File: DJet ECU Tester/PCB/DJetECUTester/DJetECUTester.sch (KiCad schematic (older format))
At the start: 27 parts, among them J1 ISP, J10 ECU3, J2 ECU1, J4 BREAKOUT, J5 12V IN, J6 MPS, J8 INJECTORS, J9 ECU2, U1 ATmega328P, Y1 FA-238 16.0000MB-C3

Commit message: Working on new schematic diagram.
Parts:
- removed D1: RED, LED_SMD:LED_PLCC-2, symbol Device:LED
- removed J4: BREAKOUT, Connector_PinHeader_2.54mm:PinHeader_2x13_P2.54mm_Vertical, symbol Connector_Generic:Conn_02x13_Odd_Even
- removed J8: INJECTORS, Britishideas:PhoenixContact_COMBICON_PT_5, symbol Connector:Screw_Terminal_01x05
- removed R5: 1K, Resistor_SMD:R_0805_2012Metric, symbol Device:R
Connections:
- net labels added: MCU_INJGROUP1-3, MCU_INJGROUP2-4, MCU_INJGROUP3-5, MCU_INJGROUP4-6
- net labels removed: ECU_DIAGGROUP13-25, START, STATUS, VAC1, VAC2
- wire segments 188 -> 159
- no-connect marks 3 -> 1
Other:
- moved on the sheet: J1, J2, J5, J6, TP5, TP6, TP7, TP8, TP9

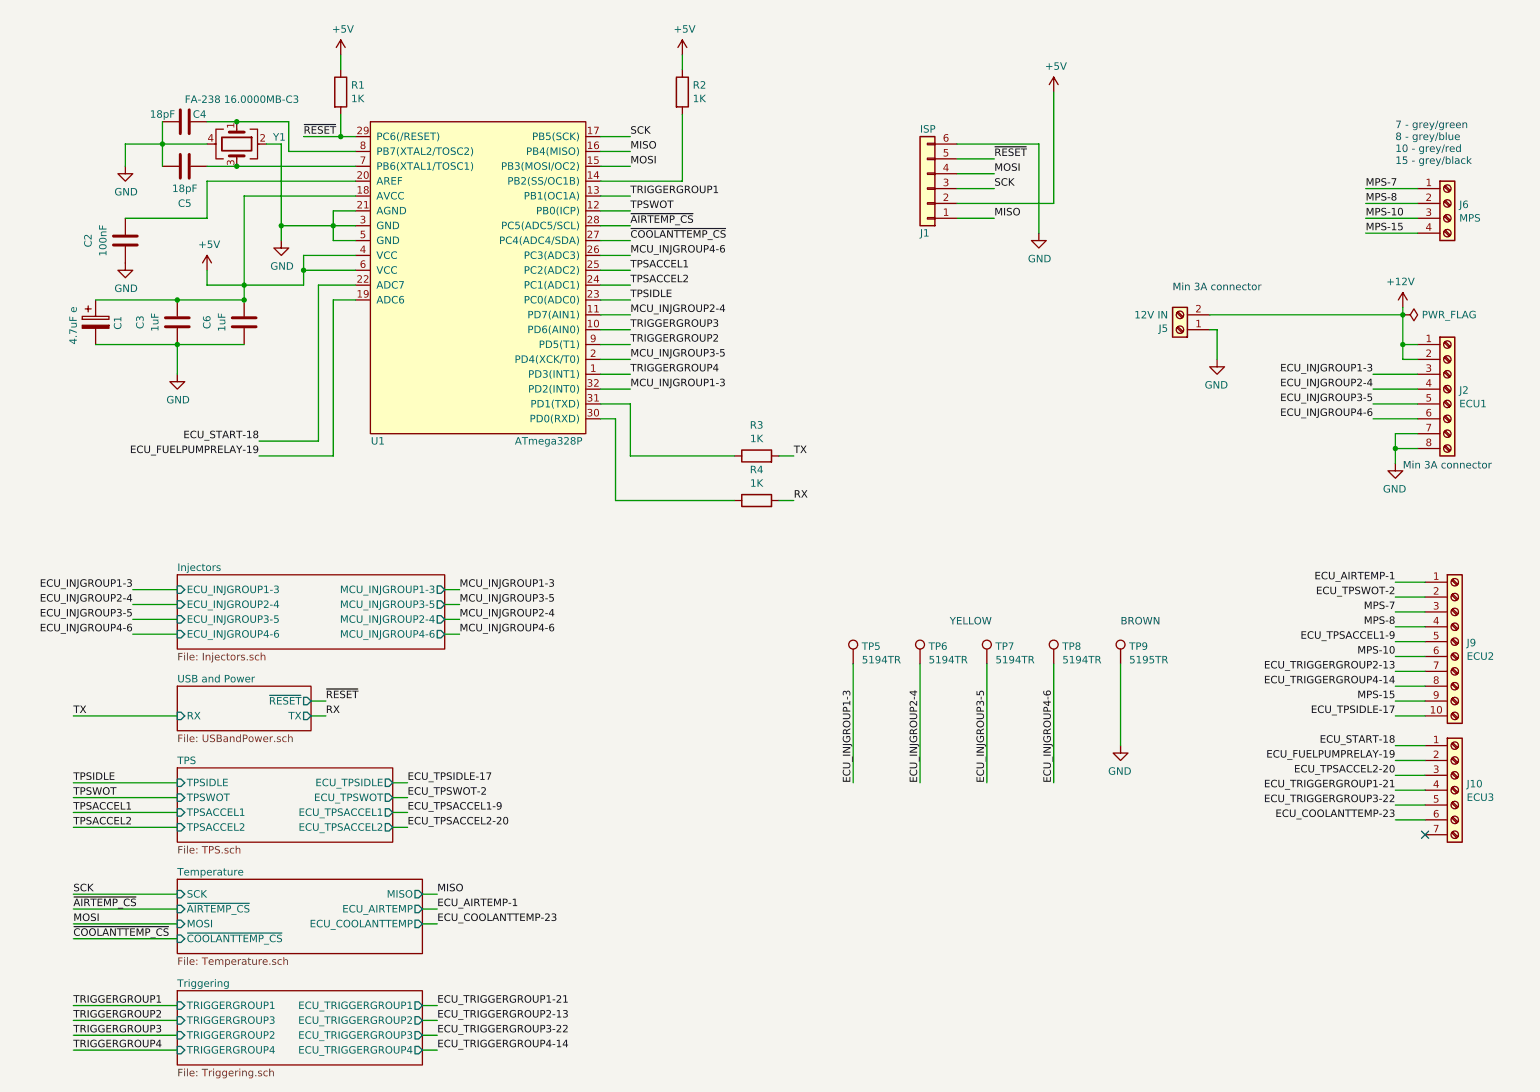
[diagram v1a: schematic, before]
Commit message: Added IO multiplexer. Working on additional coolant temperature options. Added status LED back in.
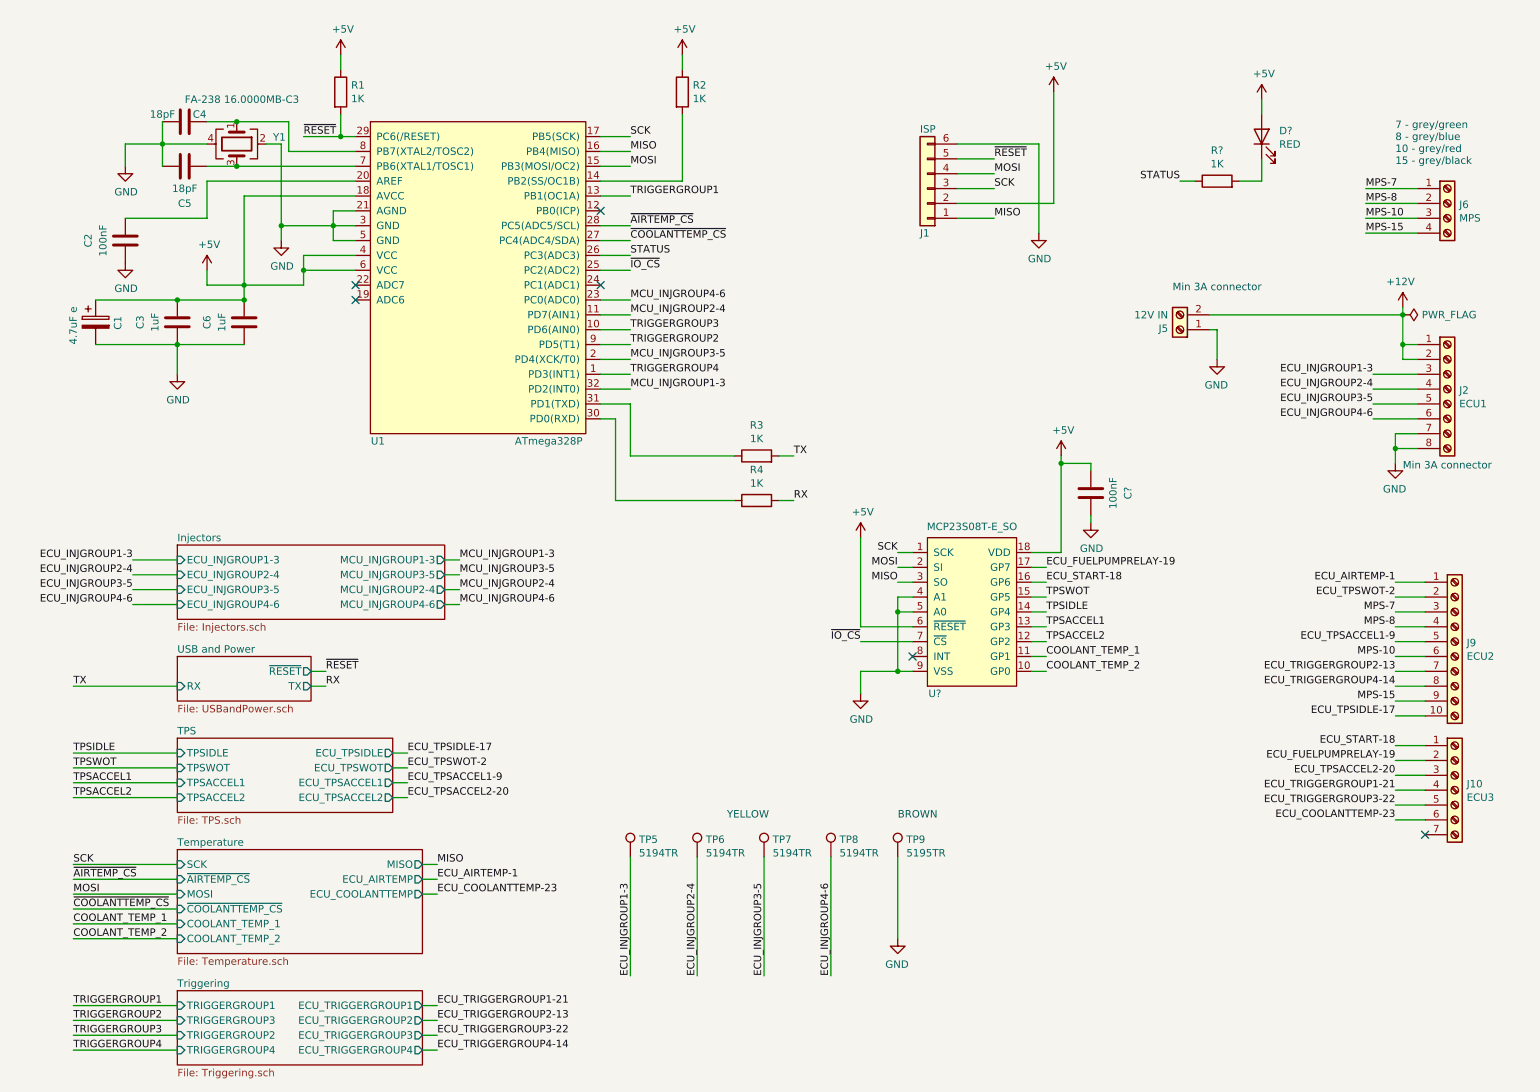
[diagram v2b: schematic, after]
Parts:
- added C?: 100nF, Capacitor_SMD:C_0805_2012Metric, symbol Device:C
- added D?: RED, LED_SMD:LED_PLCC-2, symbol Device:LED
- added R?: 1K, Resistor_SMD:R_0805_2012Metric, symbol Device:R
- added U?: MCP23S08T-E_SO, Package_SO:SOIC-18W_7.5x11.6mm_P1.27mm, symbol BritishIdeas:MCP23S08T-E_SO
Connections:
- net +5V: now also C?.2, D?.2 (A), U?.18 (VDD), U?.6 (~RESET)
- net ECU_FUELPUMPRELAY-19: now also U?.17 (GP7); no longer U1.19 (ADC6)
- net ECU_START-18: now also U?.16 (GP6); no longer U1.22 (ADC7)
- net GND: now also C?.1, U?.4 (A1), U?.5 (A0), U?.9 (VSS)
- net MCU_INJGROUP4-6: now also U1.23 (PC0(ADC0)); no longer U1.26 (PC3(ADC3))
- net MISO: now also U?.3 (SO)
- net MOSI: now also U?.2 (SI)
- net SCK: now also U?.1 (SCK)
- net TPSACCEL1: now also U?.13 (GP3); no longer U1.25 (PC2(ADC2))
- net TPSACCEL2: now also U?.12 (GP2); no longer U1.24 (PC1(ADC1))
- net TPSIDLE: now also U?.14 (GP4); no longer U1.23 (PC0(ADC0))
- net TPSWOT: now also U?.15 (GP5); no longer U1.12 (PB0(ICP))
- new net: D?.1 (K), R?.2
- new net COOLANT_TEMP_1: U?.11 (GP1)
- new net COOLANT_TEMP_2: U?.10 (GP0)
- new net STATUS: R?.1, U1.26 (PC3(ADC3))
- new net ~IO_CS: U1.25 (PC2(ADC2)), U?.7 (~CS)
- no-connect marks 1 -> 6
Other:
- moved on the sheet: TP5, TP6, TP7, TP8, TP9

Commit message: Completed new schematic.
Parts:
- added D10, D9: MBR0520LT1G, Britishideas:SOD-123, symbol Device:D
- added J4: 12V 4A IN (5.5/2.5), Connector_BarrelJack:BarrelJack_Wuerth_6941xx301002, symbol Connector:Barrel_Jack_Switch
- added R48, R49: 4k2, Resistor_SMD:R_0805_2012Metric, symbol Device:R
- added R52, R53: 10k, Resistor_SMD:R_0805_2012Metric, symbol Device:R
- gave numbers to parts that had none: 4
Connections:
- net +12V: now also J4.1
- net ECU_FUELPUMPRELAY-19: now also D10.2 (A); no longer U6.17 (GP7)
- net ECU_START-18: now also D9.2 (A); no longer U6.16 (GP6)
- net GND: now also J4.2, J4.3, R48.1, R49.1
- net ~COOLANTTEMP2_CS: now reaches U1.12 (PB0(ICP))
- net COOLANT_TEMP_1: no longer names the net of U6.11 (GP1)
- net COOLANT_TEMP_2: no longer names the net of U6.10 (GP0)
- net ~COOLANTTEMP_CS renamed ~COOLANTTEMP1_CS
- new net: D10.1 (K), R53.2
- new net: D9.1 (K), R52.2
- new net MCU_FUELPUMPRELAY-19: R49.2, R53.1, U6.17 (GP7)
- new net MCU_START-18: R48.2, R52.1, U6.16 (GP6)
- no-connect marks 6 -> 7
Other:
- note added: "Min 4A connector"
- moved on the sheet: C18, D8, J1, J2, J5, J6, R44, TP5, TP6, TP7, TP8, TP9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

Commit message: Working on new PCB.
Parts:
- added D11: RED, LED_SMD:LED_PLCC-2, symbol Device:LED
- added J7, J8: Conn_01x01, Britishideas:tabconnector-63849-1, symbol Connector_Generic:Conn_01x01
- added R54: 2k6, Resistor_SMD:R_0805_2012Metric, symbol Device:R
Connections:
- net +12V: now also J7.1 (Pin_1); no longer J2.1 (Pin_1), J2.2 (Pin_2)
- net GND: now also R54.2
- new net: D11.1 (K), R54.1
- new net ECU_PWR: D11.2 (A), J2.1 (Pin_1), J2.2 (Pin_2), J8.1 (Pin_1)
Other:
- note added: "ECU power switch"
- moved on the sheet: J1, TP5, TP6, TP7, TP8, TP9

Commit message: Completed layout. Added pull up resistors. Added ground stitching vias. Removed unused datasheets. Updated PDF schematic. Added manufacturing files. Added 3D model.
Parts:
- added R55: 1K, Resistor_SMD:R_0805_2012Metric, symbol Device:R
- added R56: 100K, Resistor_SMD:R_0805_2012Metric, symbol Device:R
- J6: manf2# (none) -> 1935187
- TP5, TP6, TP7, TP8: manf2# (none) -> 5193TR
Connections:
- net +5V: now also R55.1, R56.1; no longer U6.6 (~RESET)
- net ~IO_CS: now also R56.2
- new net: R55.2, U6.6 (~RESET)
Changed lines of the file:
@@
 Sheet 1 6
 Title "D-Jetronic ECU Tester"
-Date "2022-09-25"
+Date "2022-09-27"
 Rev "2.0"
 Comp "(C) Britishideas 2021-2022"
@@
 F 3 "~" H 10300 1550 50  0001 C CNN
 F 4 "1935792" H 10300 1550 50  0001 C CNN "manf#"
+F 5 "1935187" H 10300 1550 50  0001 C CNN "manf2#"
 	1    10300 1550
 	1    0    0    -1
@@
 F 3 "~" H 4850 6400 50  0001 C CNN
 F 4 "5194TR" H 4650 6400 50  0001 C CNN "manf#"
+F 5 "5193TR" H 4650 6400 50  0001 C CNN "manf2#"
 	1    4650 6400
 	1    0    0    -1
@@
 F 3 "~" H 5300 6400 50  0001 C CNN
 F 4 "5194TR" H 5100 6400 50  0001 C CNN "manf#"
+F 5 "5193TR" H 5100 6400 50  0001 C CNN "manf2#"
 	1    5100 6400
 	1    0    0    -1
@@
 F 3 "~" H 5750 6400 50  0001 C CNN
 F 4 "5194TR" H 5550 6400 50  0001 C CNN "manf#"
+F 5 "5193TR" H 5550 6400 50  0001 C CNN "manf2#"
 	1    5550 6400
 	1    0    0    -1
@@
 F 3 "~" H 6200 6400 50  0001 C CNN
 F 4 "5194TR" H 6000 6400 50  0001 C CNN "manf#"
+F 5 "5193TR" H 6000 6400 50  0001 C CNN "manf2#"
 	1    6000 6400
 	1    0    0    -1
@@
 Wire Wire Line
 	6550 3500 6650 3500
-Text Label 6300 4100 2    50   ~ 0
+Text Label 6000 4100 2    50   ~ 0
 ~IO_CS
 Wire Wire Line
-	6300 4100 6650 4100
+	6000 4100 6200 4100
 NoConn ~ 2900 2400
 NoConn ~ 2900 2500
@@
 L power:+5V #PWR054
 U 1 1 6335271F
-P 6300 3400
-F 0 "#PWR054" H 6300 3250 50  0001 C CNN
-F 1 "+5V" H 6315 3573 50  0000 C CNN
-F 2 "" H 6300 3400 50  0001 C CNN
-F 3 "" H 6300 3400 50  0001 C CNN
-	1    6300 3400
-	1    0    0    -1
-$EndComp
-Wire Wire Line
-	6300 3400 6300 4000
+P 6300 2850
+F 0 "#PWR054" H 6300 2700 50  0001 C CNN
+F 1 "+5V" H 6315 3023 50  0000 C CNN
+F 2 "" H 6300 2850 50  0001 C CNN
+F 3 "" H 6300 2850 50  0001 C CNN
+	1    6300 2850
+	1    0    0    -1
+$EndComp
 Wire Wire Line
 	6300 4000 6650 4000
@@
 Wire Wire Line
 	6000 1750 6000 1550
+$Comp
+L Device:R R55
+U 1 1 6334BAEB
+P 6300 3100
+F 0 "R55" H 6370 3146 50  0000 L CNN
+F 1 "1K" H 6370 3055 50  0000 L CNN
+F 2 "Resistor_SMD:R_0805_2012Metric" V 6230 3100 50  0001 C CNN
+F 3 "~" H 6300 3100 50  0001 C CNN
+	1    6300 3100
+	1    0    0    -1
+$EndComp
+Wire Wire Line
+	6300 2850 6300 2950
+Wire Wire Line
+	6300 3250 6300 4000
+$Comp
+L Device:R R56
+U 1 1 633879F7
+P 5950 3100
+F 0 "R56" H 6020 3146 50  0000 L CNN
+F 1 "100K" H 6020 3055 50  0000 L CNN
+F 2 "Resistor_SMD:R_0805_2012Metric" V 5880 3100 50  0001 C CNN
+F 3 "~" H 5950 3100 50  0001 C CNN
+	1    5950 3100
+	1    0    0    -1
+$EndComp
+Wire Wire Line
+	5950 3250 5950 3350
+Wire Wire Line
+	5950 3350 6200 3350
+Wire Wire Line
+	6200 3350 6200 4100
+Connection ~ 6200 4100
+Wire Wire Line
+	6200 4100 6650 4100
+Wire Wire Line
+	5950 2950 5950 2850
+Wire Wire Line
+	5950 2850 6300 2850
+Connection ~ 6300 2850
 $EndSCHEMATC

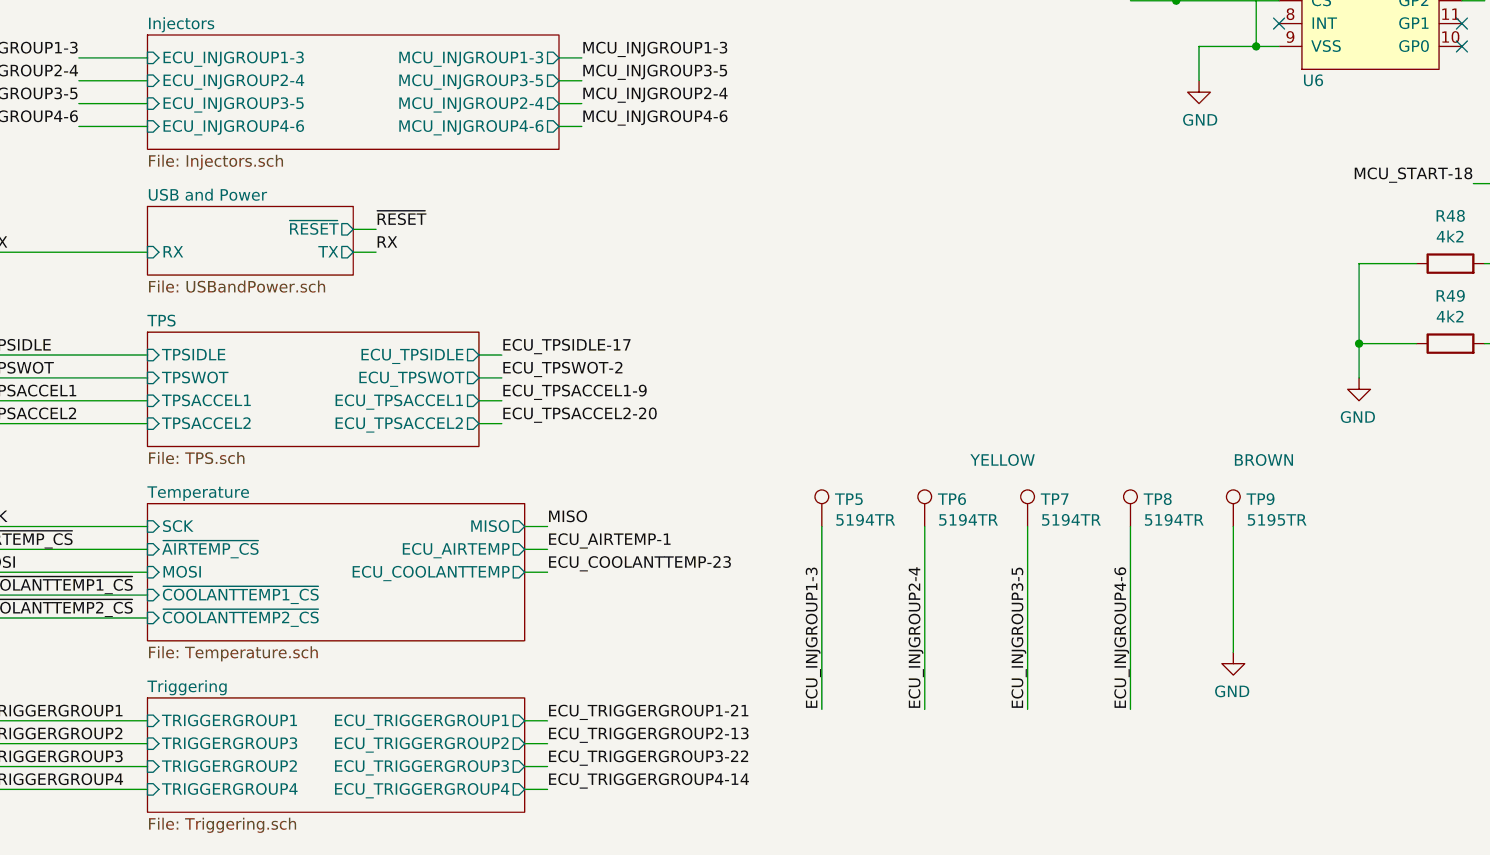
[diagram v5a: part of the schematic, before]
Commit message: Updated PCB to add resistor for fuel pump relay. Swapped trigger group signals 2 and 3 back to how they should be. Fuel pump now reports off when engine stopped.
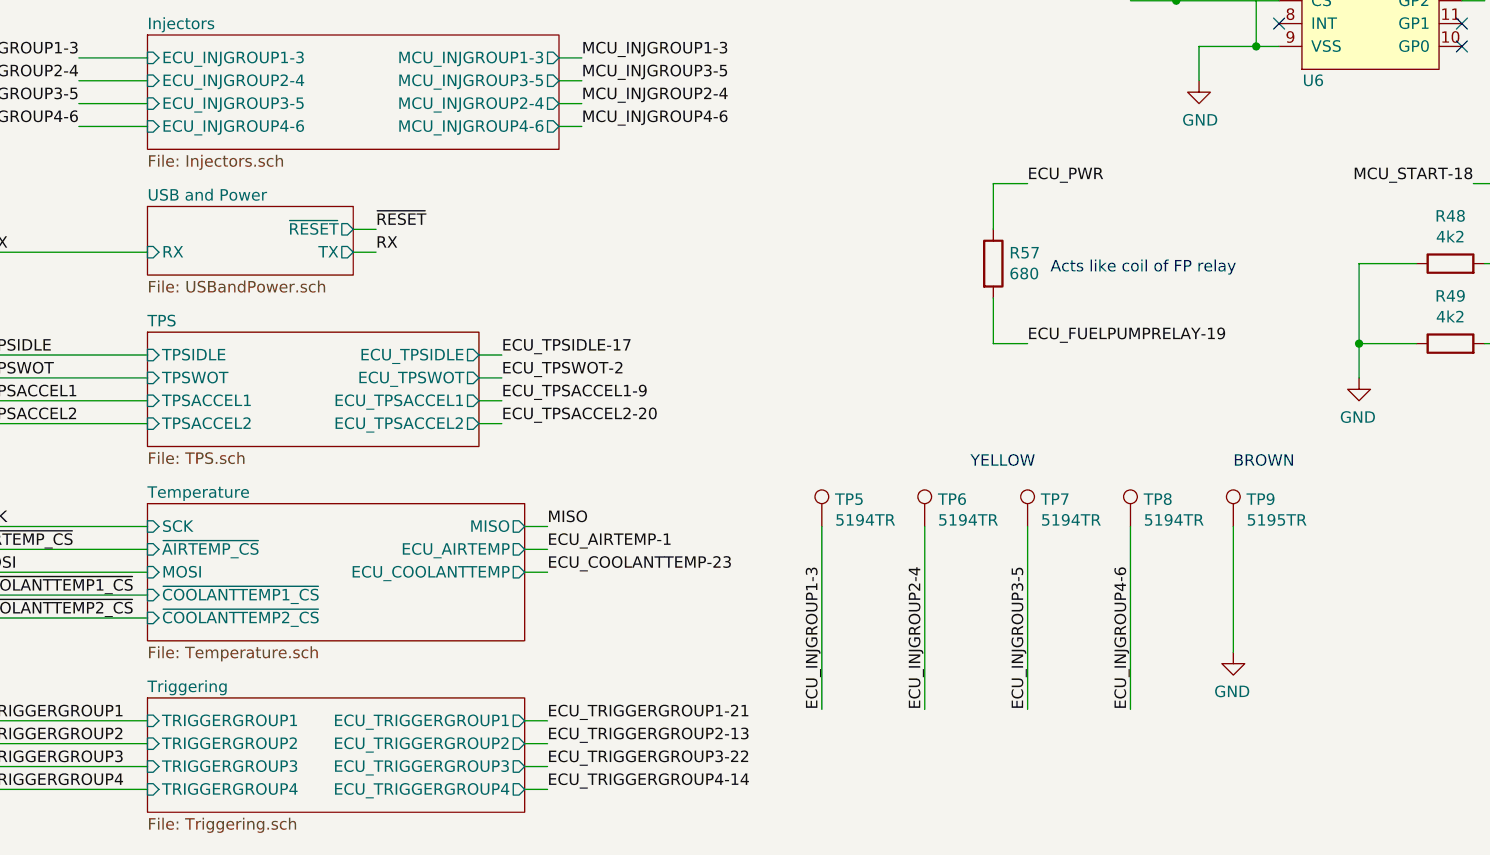
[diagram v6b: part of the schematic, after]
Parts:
- added R57: 680, Resistor_SMD:R_1206_3216Metric, symbol Device:R
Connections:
- net ECU_FUELPUMPRELAY-19: now also R57.2
- net ECU_PWR: now also R57.1
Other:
- note added: "Acts like coil of FP relay"
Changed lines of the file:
@@
 Sheet 1 6
 Title "D-Jetronic ECU Tester"
-Date "2022-09-27"
-Rev "2.0"
+Date "2022-10-14"
+Rev "2.1"
 Comp "(C) Britishideas 2021-2022"
 Comment1 ""
@@
 F5 "ECU_TRIGGERGROUP4" O R 3350 7550 50
 F6 "TRIGGERGROUP1" I L 1700 7250 50
-F7 "TRIGGERGROUP3" I L 1700 7350 50
-F8 "TRIGGERGROUP2" I L 1700 7450 50
+F7 "TRIGGERGROUP3" I L 1700 7450 50
+F8 "TRIGGERGROUP2" I L 1700 7350 50
 F9 "TRIGGERGROUP4" I L 1700 7550 50
 $EndSheet
@@
 	5950 2850 6300 2850
 Connection ~ 6300 2850
+Wire Wire Line
+	5400 4900 5400 5100
+Wire Wire Line
+	5550 4900 5400 4900
+Text Label 5550 4900 0    50   ~ 0
+ECU_PWR
+$Comp
+L Device:R R57
+U 1 1 634C12CF
+P 5400 5250
+F 0 "R57" H 5470 5296 50  0000 L CNN
+F 1 "680" H 5470 5205 50  0000 L CNN
+F 2 "Resistor_SMD:R_1206_3216Metric" V 5330 5250 50  0001 C CNN
+F 3 "~" H 5400 5250 50  0001 C CNN
+	1    5400 5250
+	1    0    0    -1
+$EndComp
+Text Label 5550 5600 0    50   ~ 0
+ECU_FUELPUMPRELAY-19
+Wire Wire Line
+	5550 5600 5400 5600
+Wire Wire Line
+	5400 5600 5400 5400
+Text Notes 5650 5300 0    50   ~ 0
+Acts like coil of FP relay
 $EndSCHEMATC
